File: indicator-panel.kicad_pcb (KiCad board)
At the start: 2 copper layers, 121.9 x 86.4 mm, 76 parts, among them P101 CONN_01X08, P102 CONN_01X08, P103 CONN_01X04, P104 CONN_01X04, U101 MAX3294, U102 STP16CP05, U103 STP16CP05, U106 STP16CP05, U108 LD1117S33CTR, U109 MAX3280, U110 MAX3280, U111 MAX3280

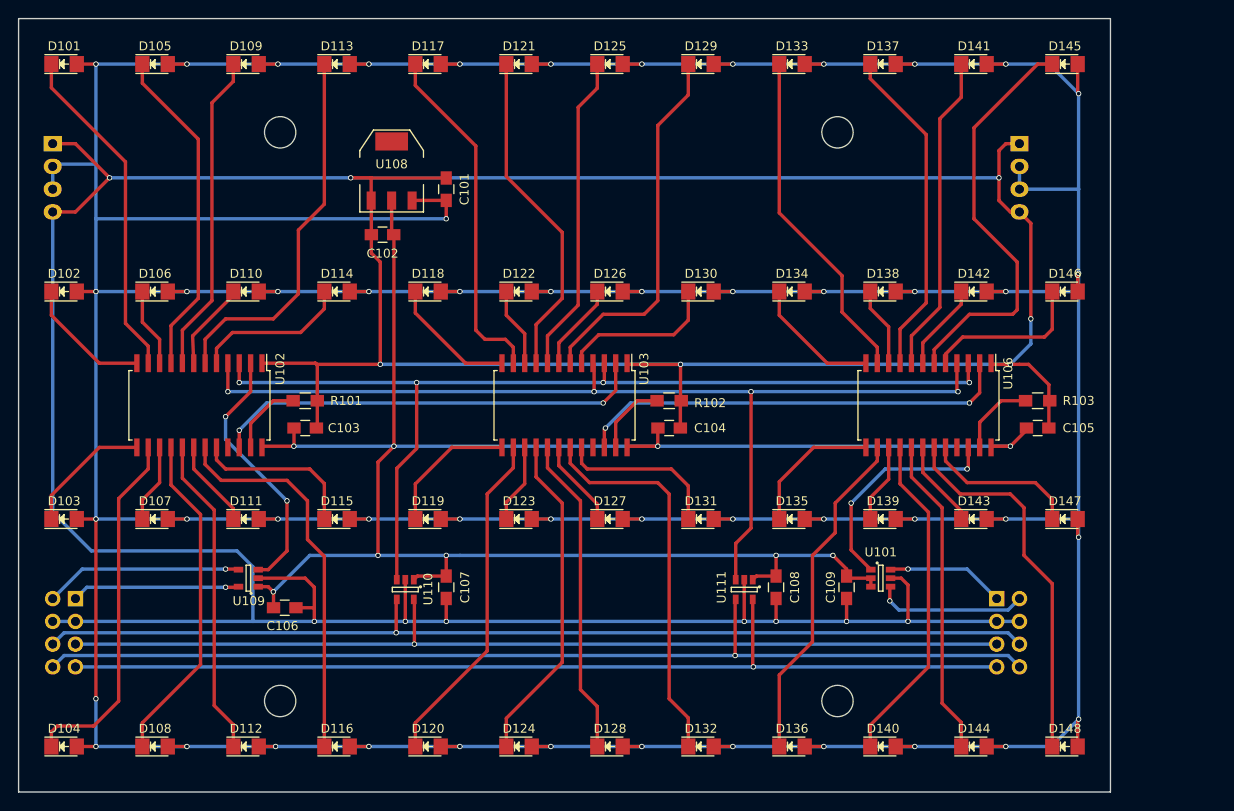
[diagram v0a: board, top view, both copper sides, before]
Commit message: Fix up connectors to carry current.
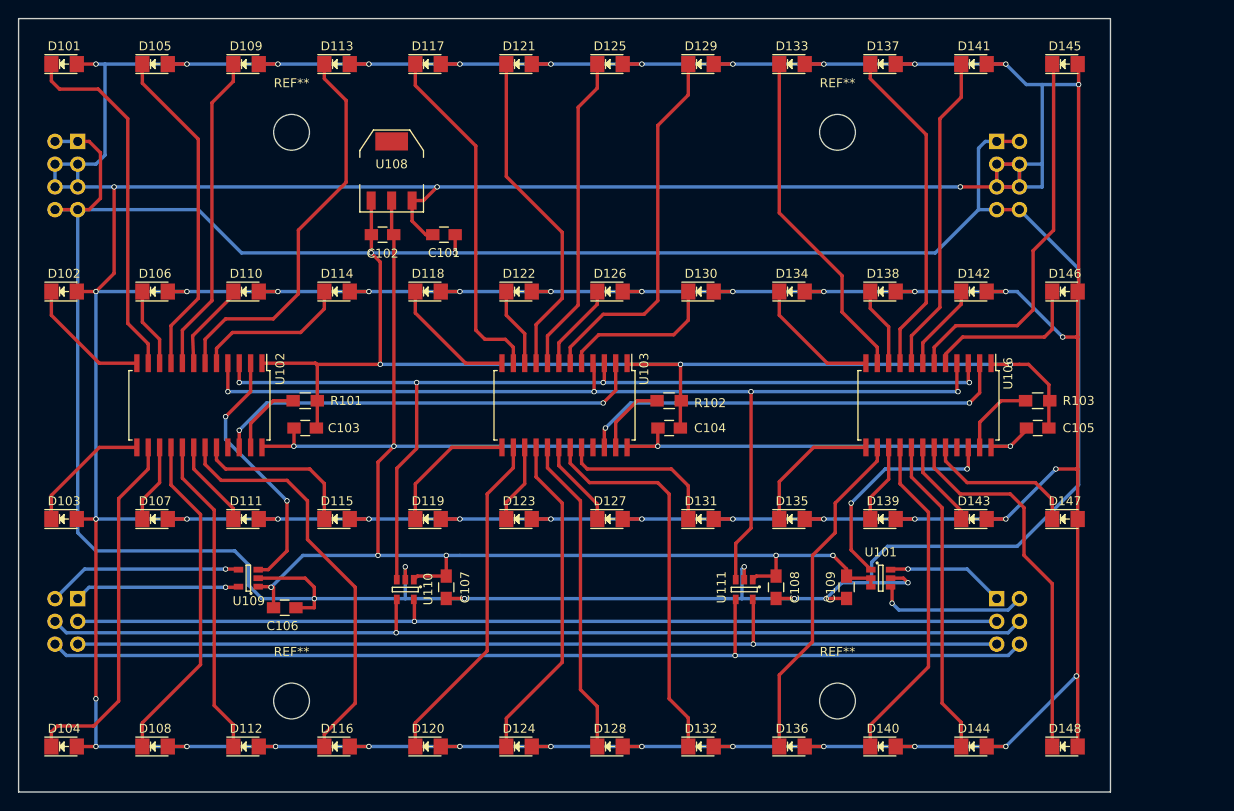
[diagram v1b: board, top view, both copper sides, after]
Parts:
- removed the REF** at (85.1, 124.5)
- removed the REF** at (85.1, 61.0)
- removed the REF** at (147.3, 61.0)
- removed the REF** at (147.3, 124.5)
- added REF**: MountingHole_4mm, Mounting_Holes:MountingHole_4mm, F.Cu at (147.3, 61.0)
- added REF**: MountingHole_4mm, Mounting_Holes:MountingHole_4mm, F.Cu at (147.3, 124.5)
- added REF**: MountingHole_4mm, Mounting_Holes:MountingHole_4mm, F.Cu at (86.4, 124.5)
- added REF**: MountingHole_4mm, Mounting_Holes:MountingHole_4mm, F.Cu at (86.4, 61.0)
- P101: value CONN_01X08 -> CONN_01X06; footprint Pin_Headers:Pin_Header_Angled_2x04 -> Pin_Headers:Pin_Header_Angled_2x03
- P102: value CONN_01X08 -> CONN_01X06; footprint Socket_Strips:Socket_Strip_Angled_2x04 -> Socket_Strips:Socket_Strip_Angled_2x03
- P103: value CONN_01X04 -> CONN_01X08; footprint Pin_Headers:Pin_Header_Angled_1x04 -> Pin_Headers:Pin_Header_Angled_2x04
- P104: value CONN_01X04 -> CONN_01X08; footprint Socket_Strips:Socket_Strip_Angled_1x04 -> Socket_Strips:Socket_Strip_Angled_2x04
- moved C101 5.09 mm to (103.4, 72.4), turned to 0 degrees
- moved P103 2.81 mm to (62.5, 62.0)
- moved P104 2.55 mm to (165.1, 62.0)
- moved P101 0.25 mm to (62.5, 113.0)
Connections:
- P101 pad 3: GND -> Net-(P101-Pad3)
- P101 pad 4: GND -> Net-(P101-Pad4)
- P102 pad 3: GND -> Net-(P101-Pad3)
- P102 pad 4: GND -> Net-(P101-Pad4)
- P103 pad 2: +12V -> GND
- P103 pad 4: GND -> +12V
- P104 pad 2: +12V -> GND
- P104 pad 4: GND -> +12V
- U110 pad 4: Net-(P101-Pad6) -> Net-(P101-Pad4)
- U110 pad 5: Net-(P101-Pad5) -> Net-(P101-Pad3)
- U111 pad 4: Net-(P101-Pad8) -> Net-(P101-Pad6)
- U111 pad 5: Net-(P101-Pad7) -> Net-(P101-Pad5)
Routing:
- net Net-(P101-Pad8): track 115.3 -> 0.00 mm, vias 1 -> 0
- net Net-(P101-Pad4): track 0.00 -> 112.5 mm, vias 0 -> 1
- net Net-(P101-Pad7): track 110.4 -> 0.00 mm, vias 1 -> 0
- net Net-(P101-Pad3): track 0.00 -> 105.1 mm, vias 0 -> 1
- net +12V: track 754.4 -> 854.3 mm, vias 50 -> 52
- net Net-(D145-Pad1): track 46.6 -> 43.0 mm
- net Net-(D116-Pad1): track 43.2 -> 46.1 mm
- net Net-(D101-Pad1): track 37.9 -> 40.4 mm
- net Net-(P101-Pad6): track 112.8 -> 115.0 mm
- net Net-(D113-Pad1): track 42.0 -> 44.1 mm
- net GND: track 501.4 -> 503.0 mm, vias 14 -> 12
- net +3V3: track 222.4 -> 223.0 mm

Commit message: Cleaned up schematic and added RK inlay.
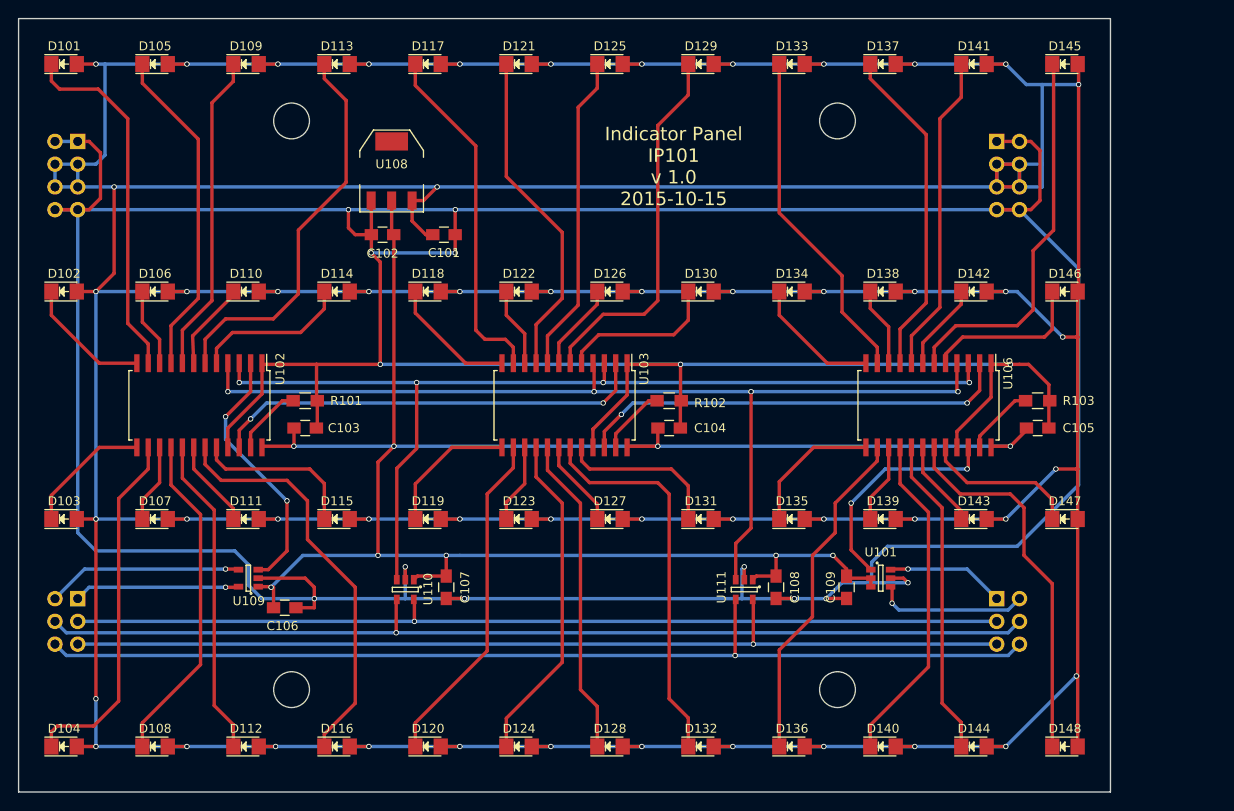
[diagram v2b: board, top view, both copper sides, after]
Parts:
- moved REF** 1.27 mm to (147.3, 59.7)
- moved REF** 1.27 mm to (86.4, 59.7)
- moved REF** 1.27 mm to (147.3, 123.2)
- moved REF** 1.27 mm to (86.4, 123.2)
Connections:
- U102 pad 21: Net-(U102-Pad21) -> GND
- U103 pad 21: Net-(U103-Pad21) -> GND
- U106 pad 21: Net-(U106-Pad21) -> GND
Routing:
- net GND: track 503.0 -> 553.2 mm, vias 12 -> 14
- net Net-(R103-Pad1): track 8.92 -> 8.03 mm
- net Net-(R102-Pad1): track 8.41 -> 7.67 mm
- net Net-(R101-Pad1): track 8.47 -> 7.87 mm
- net +12V: vias 52 -> 51
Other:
- board text added: "Indicator Panel IP101 v 1.0 2015-10-15"

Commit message: Updated pcb and rk11 inlay to .44x.88 spacing.
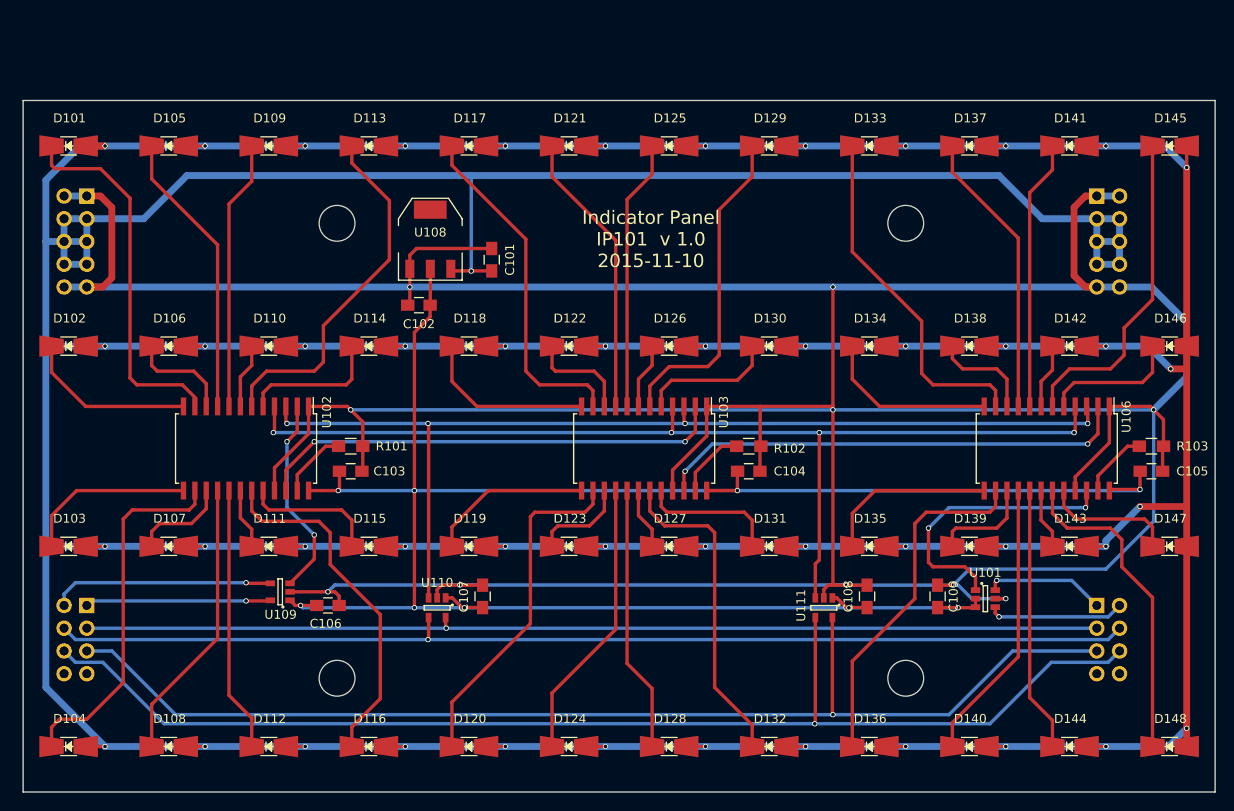
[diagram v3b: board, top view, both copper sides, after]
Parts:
- D101, D102, D103, D104, D105, D106, D107, D108, D109, D110, D111, D112, D113, D114, D115, D116, D117, D118, D119, D120, D121, D122, D123, D124, D125, D126, D127, D128, D129, D130, D131, D132, D133, D134, D135, D136, D137, D138, D139, D140, D141, D142, D143, D144, D145, D146, D147, D148: footprint LEDs:LED-1206 -> myMods.pretty:LED_SMDuniversal_0805to1206
- P101: value CONN_01X06 -> CONN_01X08; footprint Pin_Headers:Pin_Header_Angled_2x03 -> Pin_Headers:Pin_Header_Angled_2x04
- P102: value CONN_01X06 -> CONN_01X08; footprint Socket_Strips:Socket_Strip_Angled_2x03 -> Socket_Strips:Socket_Strip_Angled_2x04
- P103: value CONN_01X08 -> CONN_01X10; footprint Pin_Headers:Pin_Header_Angled_2x04 -> Pin_Headers:Pin_Header_Angled_2x05
- P104: value CONN_01X08 -> CONN_01X10; footprint Socket_Strips:Socket_Strip_Angled_2x04 -> Socket_Strips:Socket_Strip_Angled_2x05
- moved D145 14.8 mm to (184.4, 62.5)
- moved U106 14.1 mm to (170.7, 96.3)
- moved D141 14.1 mm to (173.2, 62.5)
- moved REF** 13.7 mm to (154.9, 71.1)
- moved R103 13.7 mm to (182.4, 96.0)
- moved C105 13.6 mm to (182.4, 98.8)
- moved D137 13.3 mm to (162.1, 62.5)
- moved D146 13.2 mm to (184.4, 84.8)
- moved P104 12.7 mm to (176.3, 68.1)
- moved D133 12.6 mm to (150.9, 62.5)
- moved REF** 12.5 mm to (91.4, 71.1)
- moved D142 12.3 mm to (173.2, 84.8)
- moved D147 12.1 mm to (184.4, 107.2)
- moved U101 11.9 mm to (163.8, 113.0)
- moved D129 11.9 mm to (139.7, 62.5)
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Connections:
- P103 pad 7: GND -> +12V
- P103 pad 8: GND -> +12V
- P104 pad 7: GND -> +12V
- P104 pad 8: GND -> +12V
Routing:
- net +12V: track 854.3 -> 907.8 mm, vias 51 -> 49
- net GND: track 553.2 -> 525.4 mm, vias 14 -> 10
- net Net-(P101-Pad5): track 107.6 -> 129.5 mm
- net Net-(P101-Pad6): track 115.0 -> 136.5 mm
- net +3V3: track 223.0 -> 235.8 mm
- net Net-(P101-Pad3): track 105.1 -> 114.0 mm
- net Net-(P101-Pad4): track 112.5 -> 121.4 mm
- net Net-(D132-Pad1): track 43.3 -> 36.1 mm
- net Net-(D145-Pad1): track 43.0 -> 36.4 mm
- net Net-(D116-Pad1): track 46.1 -> 39.6 mm
- net Net-(U102-Pad2): track 29.0 -> 22.6 mm
- net Net-(U101-Pad1): track 25.3 -> 31.6 mm
- net Net-(D112-Pad1): track 35.8 -> 29.6 mm
- net Net-(D148-Pad1): track 42.1 -> 36.0 mm
- net Net-(D144-Pad1): track 35.7 -> 29.6 mm
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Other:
- board size 121.9 x 86.4 mm -> 133.1 x 77.2 mm
- board text added: "Indicator Panel IP101 v 1.0 2015-11-10"
- board text removed: "Indicator Panel IP101 v 1.0 2015-10-15"

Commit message: Changed data connector use so it can be reversed with no harm.  Updated version to 1.1.
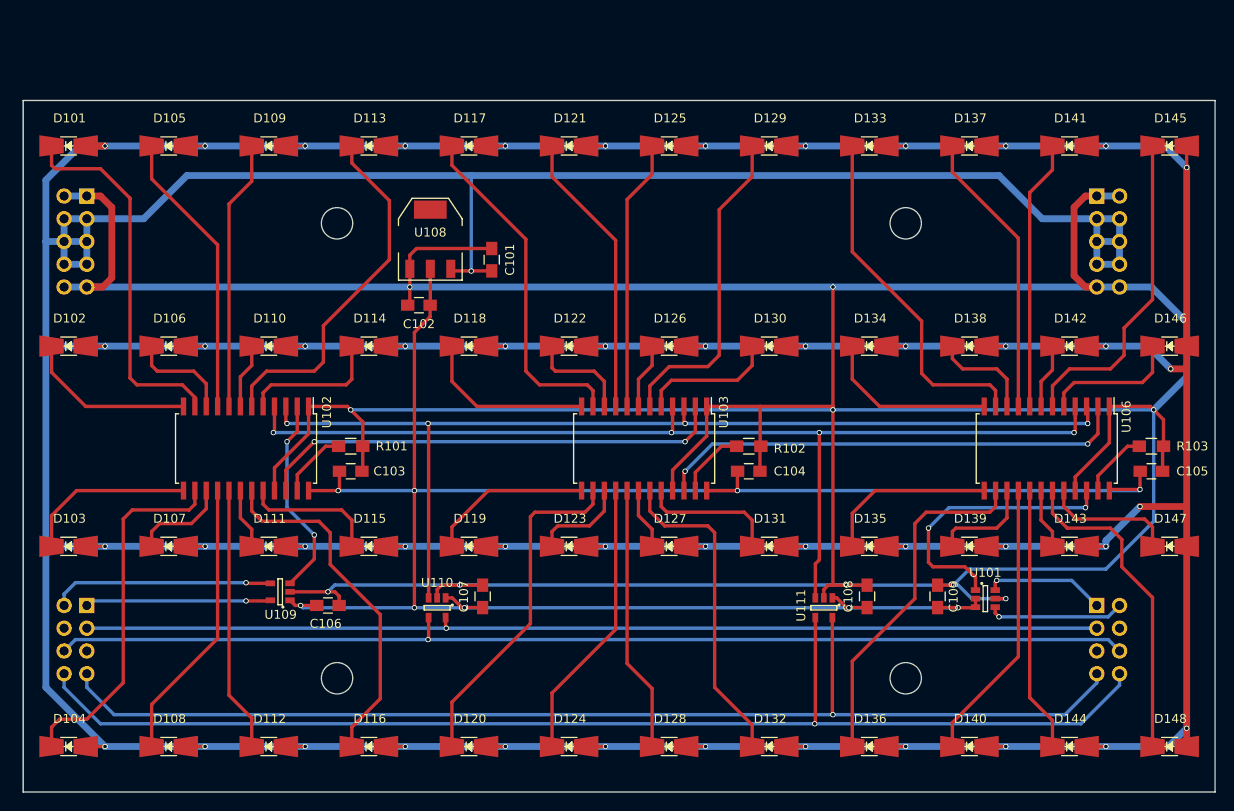
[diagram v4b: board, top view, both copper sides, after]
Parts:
- removed the REF** at (154.9, 71.1)
- removed the REF** at (154.9, 121.9)
- removed the REF** at (91.4, 121.9)
- removed the REF** at (91.4, 71.1)
- added REF**: MountingHole_3-5mm, Mounting_Holes:MountingHole_3-5mm, F.Cu at (91.4, 71.1)
- added REF**: MountingHole_3-5mm, Mounting_Holes:MountingHole_3-5mm, F.Cu at (91.4, 121.9)
- added REF**: MountingHole_3-5mm, Mounting_Holes:MountingHole_3-5mm, F.Cu at (154.9, 121.9)
- added REF**: MountingHole_3-5mm, Mounting_Holes:MountingHole_3-5mm, F.Cu at (154.9, 71.1)
- P101: footprint Pin_Headers:Pin_Header_Angled_2x04 -> Pin_Header_Angled_2x04
- P103: footprint Pin_Headers:Pin_Header_Angled_2x05 -> Pin_Header_Angled_2x05
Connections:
- P102 pad 4: Net-(P101-Pad4) -> Net-(P102-Pad4)
- P102 pad 5: Net-(P101-Pad5) -> Net-(P102-Pad5)
- P102 pad 7: Net-(P102-Pad7) -> Net-(P101-Pad7)
- P102 pad 8: Net-(P102-Pad8) -> Net-(P101-Pad8)
- U110 pad 4: Net-(P101-Pad4) -> Net-(P101-Pad6)
- U111 pad 4: Net-(P101-Pad6) -> Net-(P101-Pad8)
- U111 pad 5: Net-(P101-Pad5) -> Net-(P101-Pad7)
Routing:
- net Net-(P101-Pad8): track 0.00 -> 136.0 mm, vias 0 -> 1
- net Net-(P101-Pad5): track 129.5 -> 0.00 mm, vias 1 -> 0
- net Net-(P101-Pad7): track 0.00 -> 128.9 mm, vias 0 -> 1
- net Net-(P101-Pad4): track 121.4 -> 0.00 mm, vias 1 -> 0
- net Net-(P101-Pad6): track 136.5 -> 121.4 mm
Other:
- board text added: "Data In"
- board text added: "Data Out"
- board text added: "Power In"
- board text added: "Power Out"
- board text added: "Vintage Computer Engineering Indicator Panel IP101 v 1.1 2015-12-21"
- board text removed: "Indicator Panel IP101 v 1.0 2015-11-10"

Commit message: Added barrel connector.
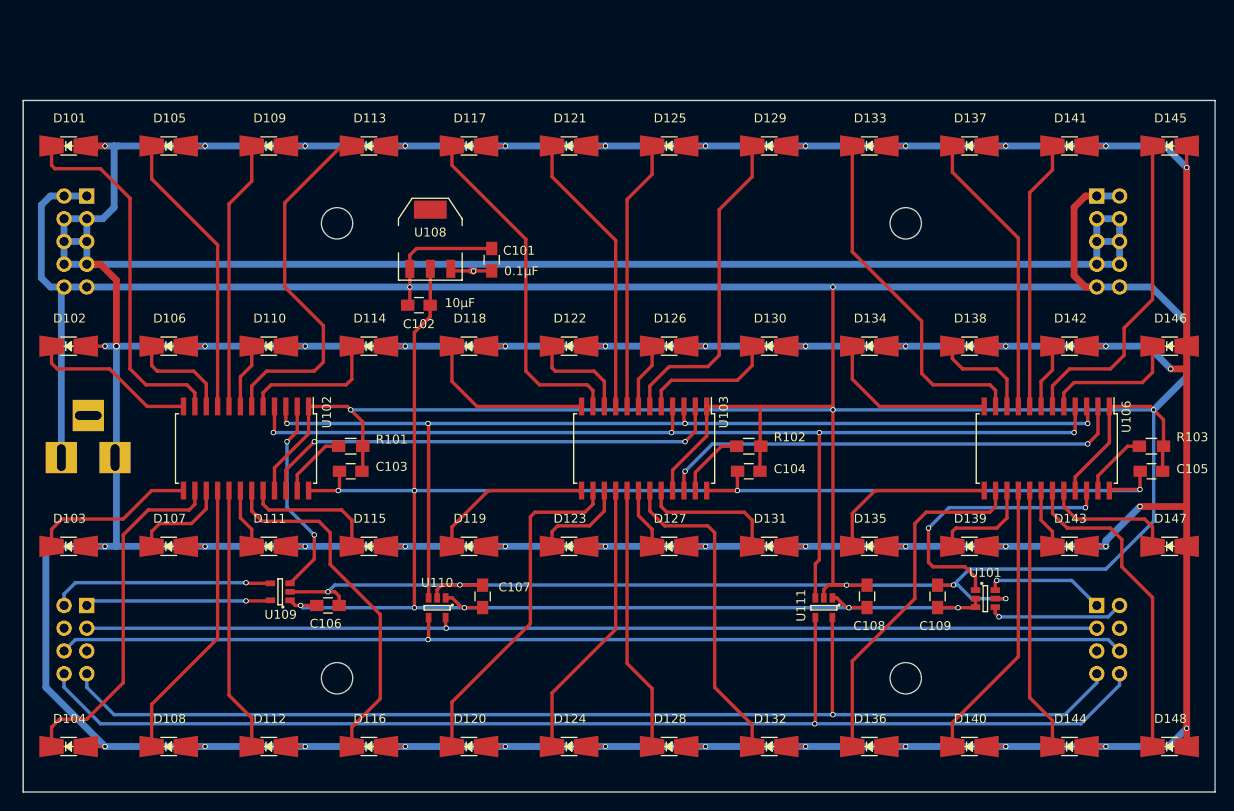
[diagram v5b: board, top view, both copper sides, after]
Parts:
- added J101: Power In, Connect:BARREL_JACK, B.Cu at (60.5, 97.3)
- C101: value 100nF -> 0.1μF
- P101: value CONN_01X08 -> Data In
- P102: value CONN_01X08 -> Data Out
- P103: value CONN_01X10 -> Power In
- P104: value CONN_01X10 -> Power Out
- R102, R103: value R -> 330Ω
- U101: value MAX3294 -> MAX3293
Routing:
- net +12V: track 907.8 -> 880.7 mm, vias 49 -> 50
- net GND: track 525.4 -> 544.2 mm
- net Net-(D104-Pad1): track 40.7 -> 39.7 mm
- net Net-(D103-Pad1): track 19.3 -> 18.4 mm
- net Net-(D113-Pad1): track 40.3 -> 41.1 mm
- net Net-(D102-Pad1): track 19.2 -> 18.6 mm
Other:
- board text added: "Vintage Computer Engineering Indicator Panel IP101 v 1.1 2016-01-14"
- board text removed: "Data In"
- board text removed: "Data Out"
- board text removed: "Power In"
- board text removed: "Power Out"
- board text removed: "Vintage Computer Engineering Indicator Panel IP101 v 1.1 2015-12-21"
